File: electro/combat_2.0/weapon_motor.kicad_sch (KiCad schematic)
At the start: 14 parts, among them J4 MOT_WPN, Q1 AO4402G, Q2 AO4402G, Q3 AO4402G, Q4 AO4402G, U5 ACS712xLCTR-20A

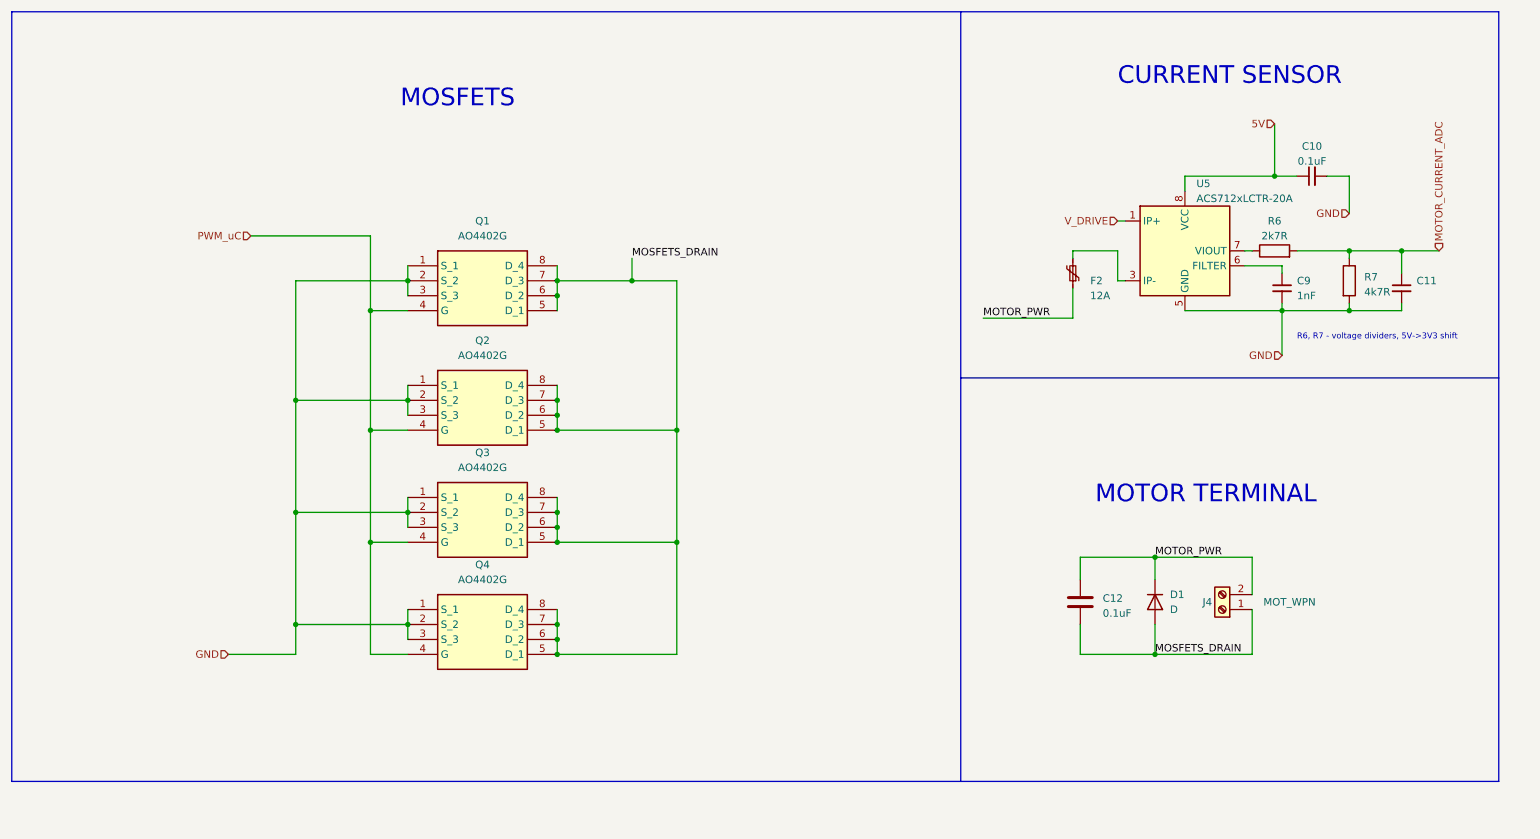
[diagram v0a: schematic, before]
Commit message: change connectors
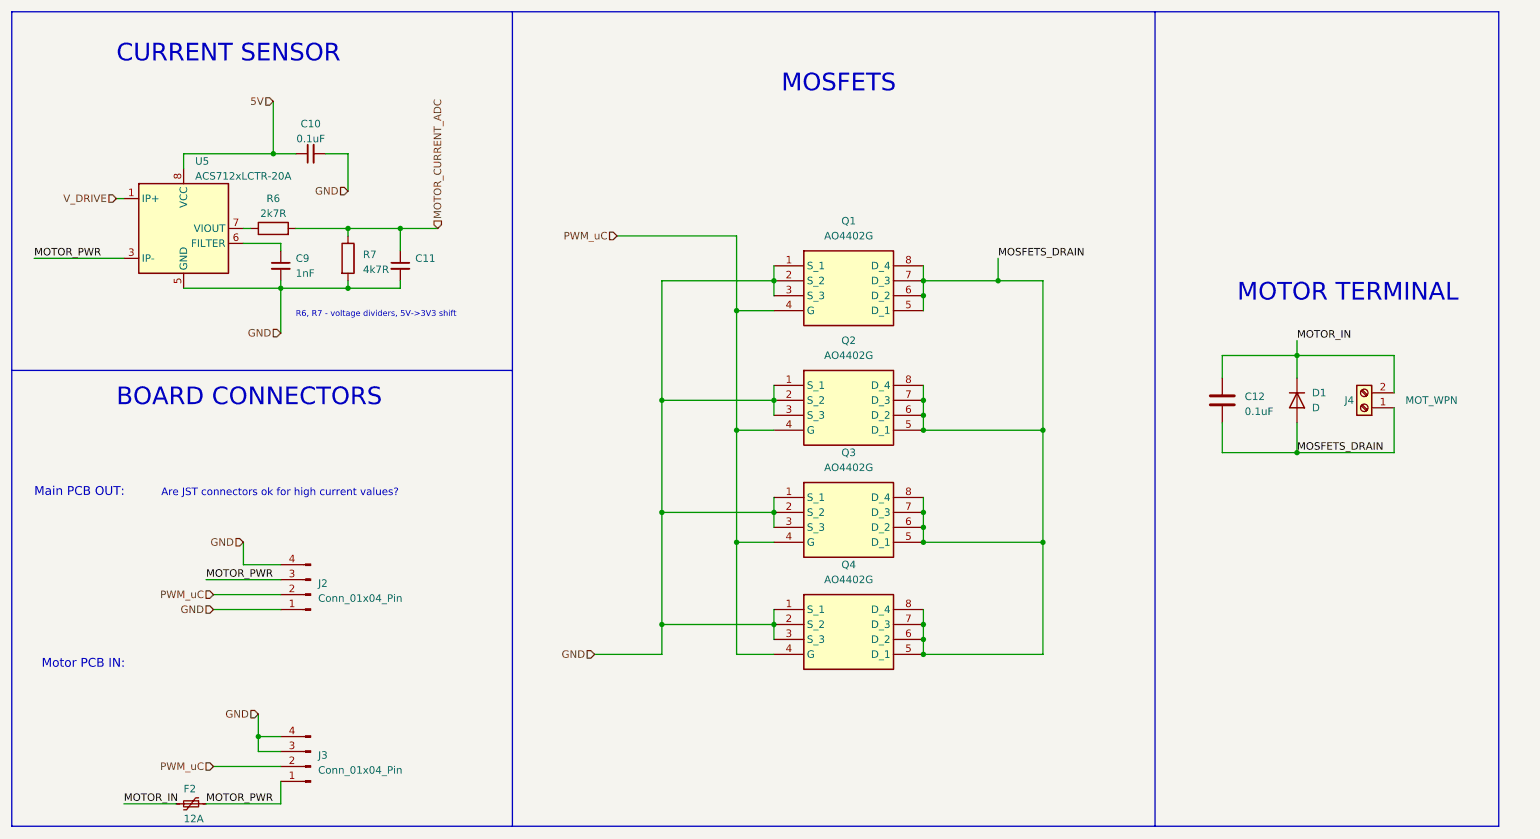
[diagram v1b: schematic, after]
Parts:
- added J2, J3: Conn_01x04_Pin, Connector_JST:JST_PH_B3B-PH-SM4-TB_1x03-1MP_P2.00mm_Vertical, symbol Connector:Conn_01x04_Pin
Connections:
- net GND: now also J2.1 (Pin_1), J2.4 (Pin_4), J3.3 (Pin_3), J3.4 (Pin_4)
- net MOTOR_PWR: now also U5.3 (IP-), U5.4 (IP-), J2.3 (Pin_3), J3.1 (Pin_1); no longer C12.1, D1.1 (K), J4.2 (Pin_2)
- net PWM_uC: now also J2.2 (Pin_2), J3.2 (Pin_2)
- new net MOTOR_IN: C12.1, D1.1 (K), F2.2, J4.2 (Pin_2)
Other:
- note added: "Are JST connectors ok for high current values?"
- note added: "BOARD CONNECTORS"
- note added: "Main PCB OUT:"
- note added: "Motor PCB IN:"
- moved on the sheet: C10, C11, C12, C9, D1, F2, J4, Q1, Q2, Q3, Q4, R6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

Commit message: almost ready pcb
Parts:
- removed J2, J3: Conn_01x04_Pin, Connector_JST:JST_PH_B3B-PH-SM4-TB_1x03-1MP_P2.00mm_Vertical, symbol Connector:Conn_01x04_Pin
- added J10, J11, J6, J7, J8, J9: Conn_01x01_Pin, TestPoint:TestPoint_Keystone_5019_Minature, symbol Connector:Conn_01x01_Pin
- C15: renamed from C9; footprint Capacitor_SMD:C_1206_3216Metric_Pad1.33x1.80mm_HandSolder -> Capacitor_SMD:C_0805_2012Metric_Pad1.18x1.45mm_HandSolder
- C16: renamed from C10; footprint Capacitor_SMD:C_0805_2012Metric -> Capacitor_SMD:C_0805_2012Metric_Pad1.18x1.45mm_HandSolder
- C17: renamed from C11; value ~ -> 1uF; footprint Capacitor_SMD:C_0805_2012Metric -> Capacitor_SMD:C_0805_2012Metric_Pad1.18x1.45mm_HandSolder
- C18: renamed from C12; footprint Capacitor_SMD:C_1206_3216Metric_Pad1.33x1.80mm_HandSolder -> Capacitor_SMD:C_0805_2012Metric_Pad1.18x1.45mm_HandSolder
- renumbered D1 to D3, J4 to J12, R6 to R7, R7 to R8, U5 to U4
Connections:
- net GND: now also J8.1 (Pin_1), J9.1 (Pin_1)
- net MOTOR_PWR: now also J11.1 (Pin_1), J6.1 (Pin_1)
- net PWM_uC: now also J10.1 (Pin_1), J7.1 (Pin_1)

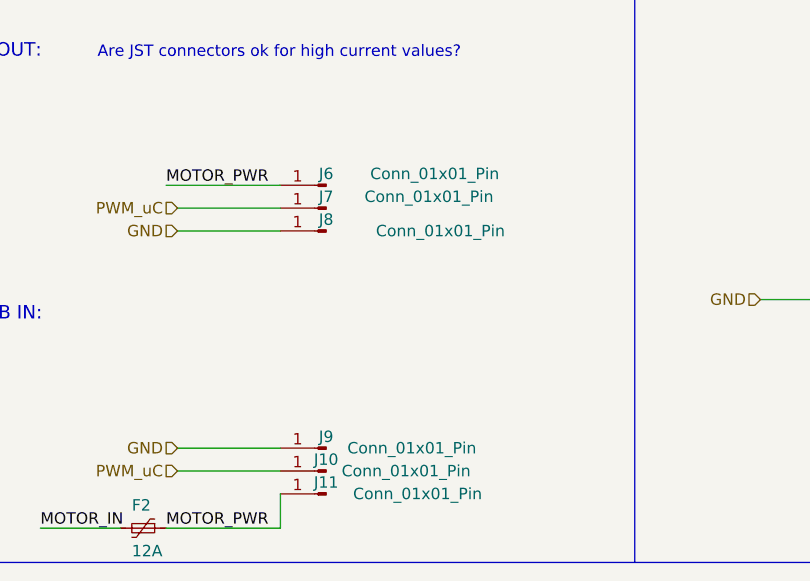
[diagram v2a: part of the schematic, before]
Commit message: Changed pads to ARKs (connecting two boards together), prepared for etching
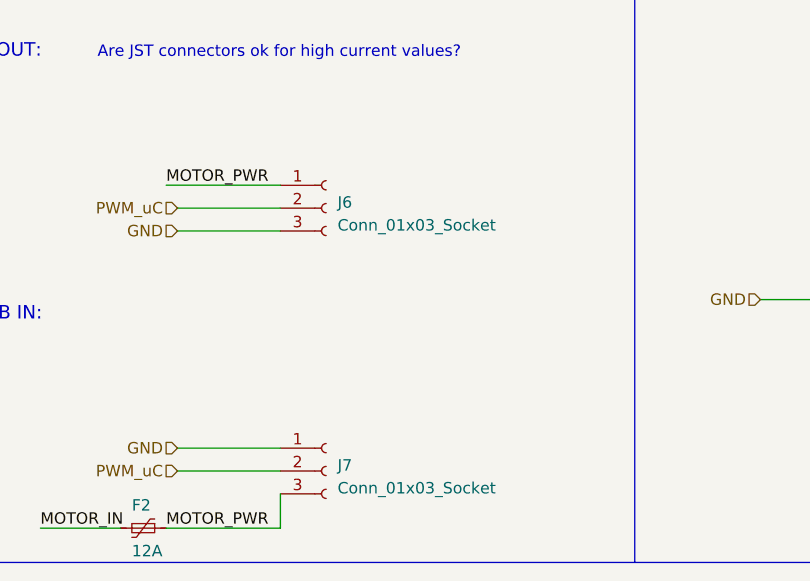
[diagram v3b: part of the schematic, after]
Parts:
- removed J10, J11, J6, J7, J8, J9: Conn_01x01_Pin, TestPoint:TestPoint_Keystone_5019_Minature, symbol Connector:Conn_01x01_Pin
- added J6, J7: Conn_01x03_Socket, TerminalBlock:TerminalBlock_Altech_AK300-3_P5.00mm, symbol Connector:Conn_01x03_Socket
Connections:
- net GND: now also J6.3 (Pin_3), J7.1 (Pin_1)
- net MOTOR_PWR: now also J6.1 (Pin_1), J7.3 (Pin_3)
- net PWM_uC: now also J6.2 (Pin_2), J7.2 (Pin_2)
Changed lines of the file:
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@@
     )
   )
-  (symbol (lib_id "Connector:Conn_01x01_Pin") (at 76.2 148.59 180) (unit 1)
-    (in_bom yes) (on_board yes) (dnp no)
-    (property "Reference" "J9" (at 76.2 147.32 0)
-      (effects (font (size 1.27 1.27)))
-    )
-    (property "Value" "Conn_01x01_Pin" (at 85.725 148.59 0)
-      (effects (font (size 1.27 1.27)))
-    )
-    (property "Footprint" "TestPoint:TestPoint_Keystone_5019_Minature" (at 76.2 148.59 0)
-      (effects (font (size 1.27 1.27)) hide)
-    )
-    (property "Datasheet" "~" (at 76.2 148.59 0)
-      (effects (font (size 1.27 1.27)) hide)
-    )
-    (pin "1")
-    (instances
-      (project "combat_2.0"
-        (path "/518cdd36-e3d2-496e-a534-90a14dea15b3/7634dbb1-8c54-4971-84cb-1ce817ae2ca8"
-          (reference "J9") (unit 1)
-        )
-      )
-    )
-  )
-  (symbol (lib_id "Connector:Conn_01x01_Pin") (at 76.2 151.13 180) (unit 1)
-    (in_bom yes) (on_board yes) (dnp no)
-    (property "Reference" "J10" (at 76.2 149.86 0)
-      (effects (font (size 1.27 1.27)))
-    )
-    (property "Value" "Conn_01x01_Pin" (at 85.09 151.13 0)
-      (effects (font (size 1.27 1.27)))
-    )
-    (property "Footprint" "TestPoint:TestPoint_Keystone_5019_Minature" (at 76.2 151.13 0)
-      (effects (font (size 1.27 1.27)) hide)
-    )
-    (property "Datasheet" "~" (at 76.2 151.13 0)
-      (effects (font (size 1.27 1.27)) hide)
-    )
-    (pin "1")
-    (instances
-      (project "combat_2.0"
-        (path "/518cdd36-e3d2-496e-a534-90a14dea15b3/7634dbb1-8c54-4971-84cb-1ce817ae2ca8"
-          (reference "J10") (unit 1)
-        )
-      )
-    )
-  )
-  (symbol (lib_id "Connector:Conn_01x01_Pin") (at 76.2 124.46 180) (unit 1)
-    (in_bom yes) (on_board yes) (dnp no)
-    (property "Reference" "J8" (at 76.2 123.19 0)
-      (effects (font (size 1.27 1.27)))
-    )
-    (property "Value" "Conn_01x01_Pin" (at 88.9 124.46 0)
-      (effects (font (size 1.27 1.27)))
-    )
-    (property "Footprint" "TestPoint:TestPoint_Keystone_5019_Minature" (at 76.2 124.46 0)
-      (effects (font (size 1.27 1.27)) hide)
-    )
-    (property "Datasheet" "~" (at 76.2 124.46 0)
-      (effects (font (size 1.27 1.27)) hide)
-    )
-    (pin "1")
-    (instances
-      (project "combat_2.0"
-        (path "/518cdd36-e3d2-496e-a534-90a14dea15b3/7634dbb1-8c54-4971-84cb-1ce817ae2ca8"
-          (reference "J8") (unit 1)
+  (symbol (lib_id "Connector:Conn_01x03_Socket") (at 76.2 121.92 0) (unit 1)
+    (in_bom yes) (on_board yes) (dnp no) (fields_autoplaced)
+    (property "Reference" "J6" (at 77.47 121.285 0)
+      (effects (font (size 1.27 1.27)) (justify left))
+    )
+    (property "Value" "Conn_01x03_Socket" (at 77.47 123.825 0)
+      (effects (font (size 1.27 1.27)) (justify left))
+    )
+    (property "Footprint" "TerminalBlock:TerminalBlock_Altech_AK300-3_P5.00mm" (at 76.2 121.92 0)
+      (effects (font (size 1.27 1.27)) hide)
+    )
+    (property "Datasheet" "~" (at 76.2 121.92 0)
+      (effects (font (size 1.27 1.27)) hide)
+    )
+    (pin "1")
+    (pin "2")
+    (pin "3")
+    (instances
+      (project "combat_2.0"
+        (path "/518cdd36-e3d2-496e-a534-90a14dea15b3/7634dbb1-8c54-4971-84cb-1ce817ae2ca8"
+          (reference "J6") (unit 1)
         )
       )
@@
     )
   )
-  (symbol (lib_id "Connector:Conn_01x01_Pin") (at 76.2 119.38 180) (unit 1)
-    (in_bom yes) (on_board yes) (dnp no)
-    (property "Reference" "J6" (at 76.2 118.11 0)
-      (effects (font (size 1.27 1.27)))
-    )
-    (property "Value" "Conn_01x01_Pin" (at 88.265 118.11 0)
-      (effects (font (size 1.27 1.27)))
-    )
-    (property "Footprint" "TestPoint:TestPoint_Keystone_5019_Minature" (at 76.2 119.38 0)
-      (effects (font (size 1.27 1.27)) hide)
-    )
-    (property "Datasheet" "~" (at 76.2 119.38 0)
-      (effects (font (size 1.27 1.27)) hide)
-    )
-    (pin "1")
-    (instances
-      (project "combat_2.0"
-        (path "/518cdd36-e3d2-496e-a534-90a14dea15b3/7634dbb1-8c54-4971-84cb-1ce817ae2ca8"
-          (reference "J6") (unit 1)
-        )
-      )
-    )
-  )
   (symbol (lib_id "AO4406AL:AO4406AL") (at 154.94 105.41 0) (unit 1)
     (in_bom yes) (on_board yes) (dnp no) (fields_autoplaced)
@@
     )
   )
-  (symbol (lib_id "Connector:Conn_01x01_Pin") (at 76.2 121.92 180) (unit 1)
-    (in_bom yes) (on_board yes) (dnp no)
-    (property "Reference" "J7" (at 76.2 120.65 0)
-      (effects (font (size 1.27 1.27)))
-    )
-    (property "Value" "Conn_01x01_Pin" (at 87.63 120.65 0)
-      (effects (font (size 1.27 1.27)))
-    )
-    (property "Footprint" "TestPoint:TestPoint_Keystone_5019_Minature" (at 76.2 121.92 0)
-      (effects (font (size 1.27 1.27)) hide)
-    )
-    (property "Datasheet" "~" (at 76.2 121.92 0)
-      (effects (font (size 1.27 1.27)) hide)
-    )
-    (pin "1")
+  (symbol (lib_id "Device:C_Small") (at 76.2 46.99 90) (unit 1)
+    (in_bom yes) (on_board yes) (dnp no) (fields_autoplaced)
+    (property "Reference" "C16" (at 76.2063 41.91 90)
+      (effects (font (size 1.27 1.27)))
+    )
+    (property "Value" "0.1uF" (at 76.2063 44.45 90)
+      (effects (font (size 1.27 1.27)))
+    )
+    (property "Footprint" "Capacitor_SMD:C_0805_2012Metric_Pad1.18x1.45mm_HandSolder" (at 76.2 46.99 0)
+      (effects (font (size 1.27 1.27)) hide)
+    )
+    (property "Datasheet" "~" (at 76.2 46.99 0)
+      (effects (font (size 1.27 1.27)) hide)
+    )
+    (pin "1")
+    (pin "2")
+    (instances
+      (project "combat_2.0"
+        (path "/518cdd36-e3d2-496e-a534-90a14dea15b3/7634dbb1-8c54-4971-84cb-1ce817ae2ca8"
+          (reference "C16") (unit 1)
+        )
+      )
+    )
+  )
+  (symbol (lib_id "Connector:Conn_01x03_Socket") (at 76.2 151.13 0) (unit 1)
+    (in_bom yes) (on_board yes) (dnp no) (fields_autoplaced)
+    (property "Reference" "J7" (at 77.47 150.495 0)
+      (effects (font (size 1.27 1.27)) (justify left))
+    )
+    (property "Value" "Conn_01x03_Socket" (at 77.47 153.035 0)
+      (effects (font (size 1.27 1.27)) (justify left))
+    )
+    (property "Footprint" "TerminalBlock:TerminalBlock_Altech_AK300-3_P5.00mm" (at 76.2 151.13 0)
+      (effects (font (size 1.27 1.27)) hide)
+    )
+    (property "Datasheet" "~" (at 76.2 151.13 0)
+      (effects (font (size 1.27 1.27)) hide)
+    )
+    (pin "1")
+    (pin "2")
+    (pin "3")
     (instances
       (project "combat_2.0"
         (path "/518cdd36-e3d2-496e-a534-90a14dea15b3/7634dbb1-8c54-4971-84cb-1ce817ae2ca8"
           (reference "J7") (unit 1)
-        )
-      )
-    )
-  )
-  (symbol (lib_id "Device:C_Small") (at 76.2 46.99 90) (unit 1)
-    (in_bom yes) (on_board yes) (dnp no) (fields_autoplaced)
-    (property "Reference" "C16" (at 76.2063 41.91 90)
-      (effects (font (size 1.27 1.27)))
-    )
-    (property "Value" "0.1uF" (at 76.2063 44.45 90)
-      (effects (font (size 1.27 1.27)))
-    )
-    (property "Footprint" "Capacitor_SMD:C_0805_2012Metric_Pad1.18x1.45mm_HandSolder" (at 76.2 46.99 0)
-      (effects (font (size 1.27 1.27)) hide)
-    )
-    (property "Datasheet" "~" (at 76.2 46.99 0)
-      (effects (font (size 1.27 1.27)) hide)
-    )
-    (pin "1")
-    (pin "2")
-    (instances
-      (project "combat_2.0"
-        (path "/518cdd36-e3d2-496e-a534-90a14dea15b3/7634dbb1-8c54-4971-84cb-1ce817ae2ca8"
-          (reference "C16") (unit 1)
         )
       )
@@
         )
       )
-    )
-  )
-  (symbol (lib_id "Connector:Conn_01x01_Pin") (at 76.2 153.67 180) (unit 1)
-    (in_bom yes) (on_board yes) (dnp no)
-    (property "Reference" "J11" (at 76.2 152.4 0)
-      (effects (font (size 1.27 1.27)))
-    )
-    (property "Value" "Conn_01x01_Pin" (at 86.36 153.67 0)
-      (effects (font (size 1.27 1.27)))
-    )
-    (property "Footprint" "TestPoint:TestPoint_Keystone_5019_Minature" (at 76.2 153.67 0)
-      (effects (font (size 1.27 1.27)) hide)
-    )
-    (property "Datasheet" "~" (at 76.2 153.67 0)
-      (effects (font (size 1.27 1.27)) hide)
-    )
-    (pin "1")
-    (instances
-      (project "combat_2.0"
-        (path "/518cdd36-e3d2-496e-a534-90a14dea15b3/7634dbb1-8c54-4971-84cb-1ce817ae2ca8"
-          (reference "J11") (unit 1)
-        )
-      )
